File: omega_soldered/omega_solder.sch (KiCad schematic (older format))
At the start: 63 parts, among them SW1 SW_Push, U1 ProMicro

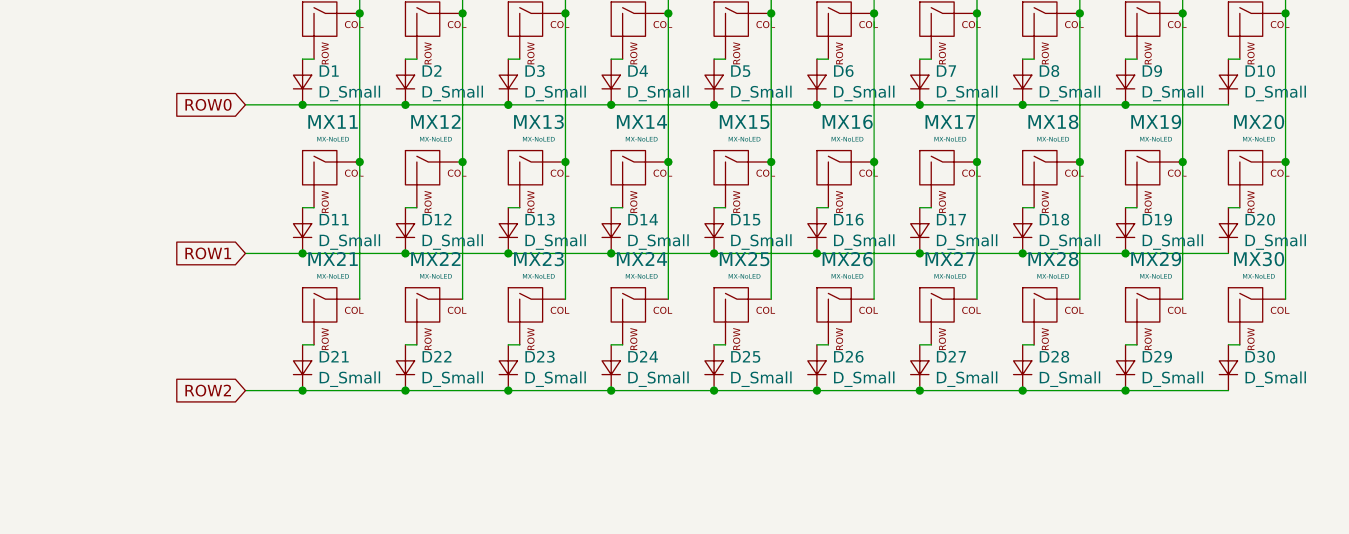
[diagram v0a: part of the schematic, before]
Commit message: add solder version
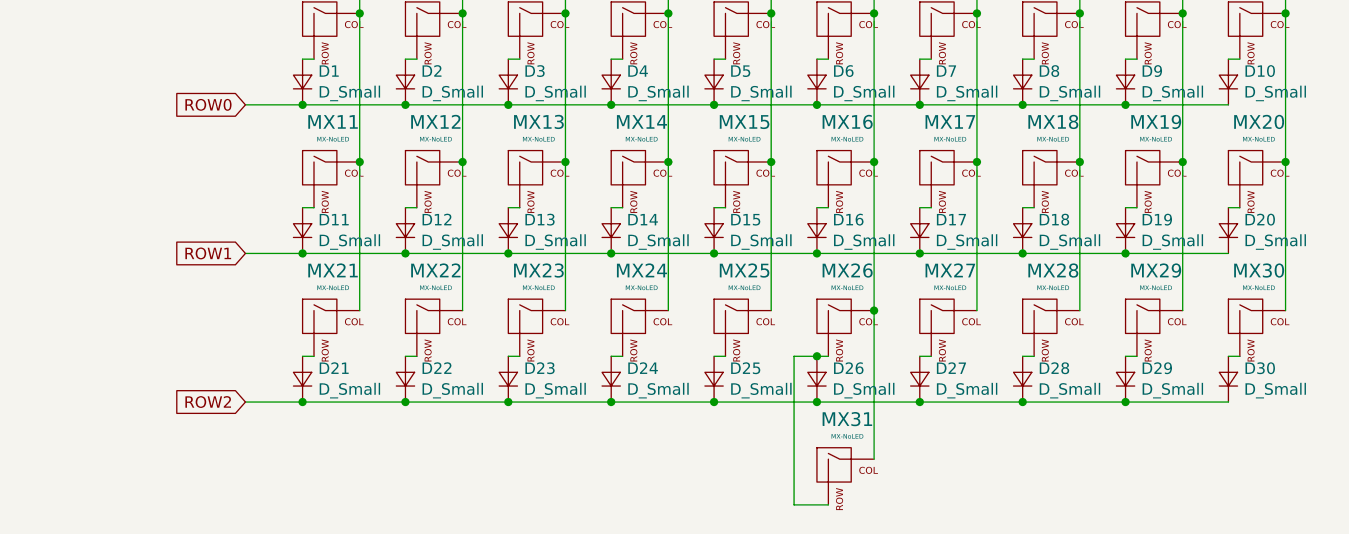
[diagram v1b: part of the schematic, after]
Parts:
- added MX31: MX-NoLED, MX_Only:MXOnly-2U-ReversedStabilizers-NoLED, symbol MX_Alps_Hybrid:MX-NoLED
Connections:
- net COL5: now also MX31.1 (COL)
- net at D26.2 (A), MX26.2 (ROW): now also MX31.2 (ROW)
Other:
- moved on the sheet: D21, D22, D23, D24, D25, D26, D27, D28, D29, D30, MX21, MX22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

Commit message: work
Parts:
- added H1, H2, H3, H4: Hole, MountingHole:MountingHole_2.2mm_M2, symbol keebio:Hole
- D1, D10, D11, D12, D13, D14, D15, D16, D17, D18, D19, D2, D20, D21, D22, D23, D24, D25, D26, D27, D28, D29, D3, D30, D4, D5, D6, D7, D8, D9: footprint Diode_THT:D_DO-35_SOD27_P3.81mm_Vertical_AnodeUp -> Keebio-Parts:Diode-Hybrid-Back
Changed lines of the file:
@@
 F 0 "D1" V 6146 1582 50  0000 R CNN
 F 1 "D_Small" V 6055 1582 50  0000 R CNN
-F 2 "Diode_THT:D_DO-35_SOD27_P3.81mm_Vertical_AnodeUp" V 6100 1650 50  0001 C CNN
+F 2 "Keebio-Parts:Diode-Hybrid-Back" V 6100 1650 50  0001 C CNN
 F 3 "~" V 6100 1650 50  0001 C CNN
 	1    6100 1650
@@
 F 0 "D11" V 6146 2232 50  0000 R CNN
 F 1 "D_Small" V 6055 2232 50  0000 R CNN
-F 2 "Diode_THT:D_DO-35_SOD27_P3.81mm_Vertical_AnodeUp" V 6100 2300 50  0001 C CNN
+F 2 "Keebio-Parts:Diode-Hybrid-Back" V 6100 2300 50  0001 C CNN
 F 3 "~" V 6100 2300 50  0001 C CNN
 	1    6100 2300
@@
 F 0 "D21" V 6146 2882 50  0000 R CNN
 F 1 "D_Small" V 6055 2882 50  0000 R CNN
-F 2 "Diode_THT:D_DO-35_SOD27_P3.81mm_Vertical_AnodeUp" V 6100 2950 50  0001 C CNN
+F 2 "Keebio-Parts:Diode-Hybrid-Back" V 6100 2950 50  0001 C CNN
 F 3 "~" V 6100 2950 50  0001 C CNN
 	1    6100 2950
@@
 F 0 "D2" V 6596 1582 50  0000 R CNN
 F 1 "D_Small" V 6505 1582 50  0000 R CNN
-F 2 "Diode_THT:D_DO-35_SOD27_P3.81mm_Vertical_AnodeUp" V 6550 1650 50  0001 C CNN
+F 2 "Keebio-Parts:Diode-Hybrid-Back" V 6550 1650 50  0001 C CNN
 F 3 "~" V 6550 1650 50  0001 C CNN
 	1    6550 1650
@@
 F 0 "D12" V 6596 2232 50  0000 R CNN
 F 1 "D_Small" V 6505 2232 50  0000 R CNN
-F 2 "Diode_THT:D_DO-35_SOD27_P3.81mm_Vertical_AnodeUp" V 6550 2300 50  0001 C CNN
+F 2 "Keebio-Parts:Diode-Hybrid-Back" V 6550 2300 50  0001 C CNN
 F 3 "~" V 6550 2300 50  0001 C CNN
 	1    6550 2300
@@
 F 0 "D22" V 6596 2882 50  0000 R CNN
 F 1 "D_Small" V 6505 2882 50  0000 R CNN
-F 2 "Diode_THT:D_DO-35_SOD27_P3.81mm_Vertical_AnodeUp" V 6550 2950 50  0001 C CNN
+F 2 "Keebio-Parts:Diode-Hybrid-Back" V 6550 2950 50  0001 C CNN
 F 3 "~" V 6550 2950 50  0001 C CNN
 	1    6550 2950
@@
 F 0 "D3" V 7046 1582 50  0000 R CNN
 F 1 "D_Small" V 6955 1582 50  0000 R CNN
-F 2 "Diode_THT:D_DO-35_SOD27_P3.81mm_Vertical_AnodeUp" V 7000 1650 50  0001 C CNN
+F 2 "Keebio-Parts:Diode-Hybrid-Back" V 7000 1650 50  0001 C CNN
 F 3 "~" V 7000 1650 50  0001 C CNN
 	1    7000 1650
@@
 F 0 "D13" V 7046 2232 50  0000 R CNN
 F 1 "D_Small" V 6955 2232 50  0000 R CNN
-F 2 "Diode_THT:D_DO-35_SOD27_P3.81mm_Vertical_AnodeUp" V 7000 2300 50  0001 C CNN
+F 2 "Keebio-Parts:Diode-Hybrid-Back" V 7000 2300 50  0001 C CNN
 F 3 "~" V 7000 2300 50  0001 C CNN
 	1    7000 2300
@@
 F 0 "D23" V 7046 2882 50  0000 R CNN
 F 1 "D_Small" V 6955 2882 50  0000 R CNN
-F 2 "Diode_THT:D_DO-35_SOD27_P3.81mm_Vertical_AnodeUp" V 7000 2950 50  0001 C CNN
+F 2 "Keebio-Parts:Diode-Hybrid-Back" V 7000 2950 50  0001 C CNN
 F 3 "~" V 7000 2950 50  0001 C CNN
 	1    7000 2950
@@
 F 0 "D4" V 7496 1582 50  0000 R CNN
 F 1 "D_Small" V 7405 1582 50  0000 R CNN
-F 2 "Diode_THT:D_DO-35_SOD27_P3.81mm_Vertical_AnodeUp" V 7450 1650 50  0001 C CNN
+F 2 "Keebio-Parts:Diode-Hybrid-Back" V 7450 1650 50  0001 C CNN
 F 3 "~" V 7450 1650 50  0001 C CNN
 	1    7450 1650
@@
 F 0 "D14" V 7496 2232 50  0000 R CNN
 F 1 "D_Small" V 7405 2232 50  0000 R CNN
-F 2 "Diode_THT:D_DO-35_SOD27_P3.81mm_Vertical_AnodeUp" V 7450 2300 50  0001 C CNN
+F 2 "Keebio-Parts:Diode-Hybrid-Back" V 7450 2300 50  0001 C CNN
 F 3 "~" V 7450 2300 50  0001 C CNN
 	1    7450 2300
@@
 F 0 "D24" V 7496 2882 50  0000 R CNN
 F 1 "D_Small" V 7405 2882 50  0000 R CNN
-F 2 "Diode_THT:D_DO-35_SOD27_P3.81mm_Vertical_AnodeUp" V 7450 2950 50  0001 C CNN
+F 2 "Keebio-Parts:Diode-Hybrid-Back" V 7450 2950 50  0001 C CNN
 F 3 "~" V 7450 2950 50  0001 C CNN
 	1    7450 2950
@@
 F 0 "D5" V 7946 1582 50  0000 R CNN
 F 1 "D_Small" V 7855 1582 50  0000 R CNN
-F 2 "Diode_THT:D_DO-35_SOD27_P3.81mm_Vertical_AnodeUp" V 7900 1650 50  0001 C CNN
+F 2 "Keebio-Parts:Diode-Hybrid-Back" V 7900 1650 50  0001 C CNN
 F 3 "~" V 7900 1650 50  0001 C CNN
 	1    7900 1650
@@
 F 0 "D15" V 7946 2232 50  0000 R CNN
 F 1 "D_Small" V 7855 2232 50  0000 R CNN
-F 2 "Diode_THT:D_DO-35_SOD27_P3.81mm_Vertical_AnodeUp" V 7900 2300 50  0001 C CNN
+F 2 "Keebio-Parts:Diode-Hybrid-Back" V 7900 2300 50  0001 C CNN
 F 3 "~" V 7900 2300 50  0001 C CNN
 	1    7900 2300
@@
 F 0 "D25" V 7946 2882 50  0000 R CNN
 F 1 "D_Small" V 7855 2882 50  0000 R CNN
-F 2 "Diode_THT:D_DO-35_SOD27_P3.81mm_Vertical_AnodeUp" V 7900 2950 50  0001 C CNN
+F 2 "Keebio-Parts:Diode-Hybrid-Back" V 7900 2950 50  0001 C CNN
 F 3 "~" V 7900 2950 50  0001 C CNN
 	1    7900 2950
@@
 F 0 "D6" V 8396 1582 50  0000 R CNN
 F 1 "D_Small" V 8305 1582 50  0000 R CNN
-F 2 "Diode_THT:D_DO-35_SOD27_P3.81mm_Vertical_AnodeUp" V 8350 1650 50  0001 C CNN
+F 2 "Keebio-Parts:Diode-Hybrid-Back" V 8350 1650 50  0001 C CNN
 F 3 "~" V 8350 1650 50  0001 C CNN
 	1    8350 1650
@@
 F 0 "D16" V 8396 2232 50  0000 R CNN
 F 1 "D_Small" V 8305 2232 50  0000 R CNN
-F 2 "Diode_THT:D_DO-35_SOD27_P3.81mm_Vertical_AnodeUp" V 8350 2300 50  0001 C CNN
+F 2 "Keebio-Parts:Diode-Hybrid-Back" V 8350 2300 50  0001 C CNN
 F 3 "~" V 8350 2300 50  0001 C CNN
 	1    8350 2300
@@
 F 0 "D7" V 8846 1582 50  0000 R CNN
 F 1 "D_Small" V 8755 1582 50  0000 R CNN
-F 2 "Diode_THT:D_DO-35_SOD27_P3.81mm_Vertical_AnodeUp" V 8800 1650 50  0001 C CNN
+F 2 "Keebio-Parts:Diode-Hybrid-Back" V 8800 1650 50  0001 C CNN
 F 3 "~" V 8800 1650 50  0001 C CNN
 	1    8800 1650
@@
 F 0 "D17" V 8846 2232 50  0000 R CNN
 F 1 "D_Small" V 8755 2232 50  0000 R CNN
-F 2 "Diode_THT:D_DO-35_SOD27_P3.81mm_Vertical_AnodeUp" V 8800 2300 50  0001 C CNN
+F 2 "Keebio-Parts:Diode-Hybrid-Back" V 8800 2300 50  0001 C CNN
 F 3 "~" V 8800 2300 50  0001 C CNN
 	1    8800 2300
@@
 F 0 "D27" V 8846 2882 50  0000 R CNN
 F 1 "D_Small" V 8755 2882 50  0000 R CNN
-F 2 "Diode_THT:D_DO-35_SOD27_P3.81mm_Vertical_AnodeUp" V 8800 2950 50  0001 C CNN
+F 2 "Keebio-Parts:Diode-Hybrid-Back" V 8800 2950 50  0001 C CNN
 F 3 "~" V 8800 2950 50  0001 C CNN
 	1    8800 2950
@@
 F 0 "D8" V 9296 1582 50  0000 R CNN
 F 1 "D_Small" V 9205 1582 50  0000 R CNN
-F 2 "Diode_THT:D_DO-35_SOD27_P3.81mm_Vertical_AnodeUp" V 9250 1650 50  0001 C CNN
+F 2 "Keebio-Parts:Diode-Hybrid-Back" V 9250 1650 50  0001 C CNN
 F 3 "~" V 9250 1650 50  0001 C CNN
 	1    9250 1650
@@
 F 0 "D18" V 9296 2232 50  0000 R CNN
 F 1 "D_Small" V 9205 2232 50  0000 R CNN
-F 2 "Diode_THT:D_DO-35_SOD27_P3.81mm_Vertical_AnodeUp" V 9250 2300 50  0001 C CNN
+F 2 "Keebio-Parts:Diode-Hybrid-Back" V 9250 2300 50  0001 C CNN
 F 3 "~" V 9250 2300 50  0001 C CNN
 	1    9250 2300
@@
 F 0 "D28" V 9296 2882 50  0000 R CNN
 F 1 "D_Small" V 9205 2882 50  0000 R CNN
-F 2 "Diode_THT:D_DO-35_SOD27_P3.81mm_Vertical_AnodeUp" V 9250 2950 50  0001 C CNN
+F 2 "Keebio-Parts:Diode-Hybrid-Back" V 9250 2950 50  0001 C CNN
 F 3 "~" V 9250 2950 50  0001 C CNN
 	1    9250 2950
@@
 F 0 "D9" V 9746 1582 50  0000 R CNN
 F 1 "D_Small" V 9655 1582 50  0000 R CNN
-F 2 "Diode_THT:D_DO-35_SOD27_P3.81mm_Vertical_AnodeUp" V 9700 1650 50  0001 C CNN
+F 2 "Keebio-Parts:Diode-Hybrid-Back" V 9700 1650 50  0001 C CNN
 F 3 "~" V 9700 1650 50  0001 C CNN
 	1    9700 1650
@@
 F 0 "D19" V 9746 2232 50  0000 R CNN
 F 1 "D_Small" V 9655 2232 50  0000 R CNN
-F 2 "Diode_THT:D_DO-35_SOD27_P3.81mm_Vertical_AnodeUp" V 9700 2300 50  0001 C CNN
+F 2 "Keebio-Parts:Diode-Hybrid-Back" V 9700 2300 50  0001 C CNN
 F 3 "~" V 9700 2300 50  0001 C CNN
 	1    9700 2300
@@
 F 0 "D29" V 9746 2882 50  0000 R CNN
 F 1 "D_Small" V 9655 2882 50  0000 R CNN
-F 2 "Diode_THT:D_DO-35_SOD27_P3.81mm_Vertical_AnodeUp" V 9700 2950 50  0001 C CNN
+F 2 "Keebio-Parts:Diode-Hybrid-Back" V 9700 2950 50  0001 C CNN
 F 3 "~" V 9700 2950 50  0001 C CNN
 	1    9700 2950
@@
 F 0 "D10" V 10196 1582 50  0000 R CNN
 F 1 "D_Small" V 10105 1582 50  0000 R CNN
-F 2 "Diode_THT:D_DO-35_SOD27_P3.81mm_Vertical_AnodeUp" V 10150 1650 50  0001 C CNN
+F 2 "Keebio-Parts:Diode-Hybrid-Back" V 10150 1650 50  0001 C CNN
 F 3 "~" V 10150 1650 50  0001 C CNN
 	1    10150 1650
@@
 F 0 "D20" V 10196 2232 50  0000 R CNN
 F 1 "D_Small" V 10105 2232 50  0000 R CNN
-F 2 "Diode_THT:D_DO-35_SOD27_P3.81mm_Vertical_AnodeUp" V 10150 2300 50  0001 C CNN
+F 2 "Keebio-Parts:Diode-Hybrid-Back" V 10150 2300 50  0001 C CNN
 F 3 "~" V 10150 2300 50  0001 C CNN
 	1    10150 2300
@@
 F 0 "D30" V 10196 2882 50  0000 R CNN
 F 1 "D_Small" V 10105 2882 50  0000 R CNN
-F 2 "Diode_THT:D_DO-35_SOD27_P3.81mm_Vertical_AnodeUp" V 10150 2950 50  0001 C CNN
+F 2 "Keebio-Parts:Diode-Hybrid-Back" V 10150 2950 50  0001 C CNN
 F 3 "~" V 10150 2950 50  0001 C CNN
 	1    10150 2950
@@
 F 0 "D26" V 8396 2882 50  0000 R CNN
 F 1 "D_Small" V 8305 2882 50  0000 R CNN
-F 2 "Diode_THT:D_DO-35_SOD27_P3.81mm_Vertical_AnodeUp" V 8350 2950 50  0001 C CNN
+F 2 "Keebio-Parts:Diode-Hybrid-Back" V 8350 2950 50  0001 C CNN
 F 3 "~" V 8350 2950 50  0001 C CNN
 	1    8350 2950
@@
 	9950 2000 9950 2650
 Connection ~ 9950 2000
+$Comp
+L keebio:Hole H1
+U 1 1 5F08444E
+P 4350 3500
+F 0 "H1" H 4536 3553 60  0000 L CNN
+F 1 "Hole" H 4536 3447 60  0000 L CNN
+F 2 "MountingHole:MountingHole_2.2mm_M2" H 4350 3500 60  0001 C CNN
+F 3 "" H 4350 3500 60  0001 C CNN
+	1    4350 3500
+	1    0    0    -1
+$EndComp
+$Comp
+L keebio:Hole H2
+U 1 1 5F084F55
+P 4950 3500
+F 0 "H2" H 5136 3553 60  0000 L CNN
+F 1 "Hole" H 5136 3447 60  0000 L CNN
+F 2 "MountingHole:MountingHole_2.2mm_M2" H 4950 3500 60  0001 C CNN
+F 3 "" H 4950 3500 60  0001 C CNN
+	1    4950 3500
+	1    0    0    -1
+$EndComp
+$Comp
+L keebio:Hole H4
+U 1 1 5F085599
+P 4950 3900
+F 0 "H4" H 5136 3953 60  0000 L CNN
+F 1 "Hole" H 5136 3847 60  0000 L CNN
+F 2 "MountingHole:MountingHole_2.2mm_M2" H 4950 3900 60  0001 C CNN
+F 3 "" H 4950 3900 60  0001 C CNN
+	1    4950 3900
+	1    0    0    -1
+$EndComp
+$Comp
+L keebio:Hole H3
+U 1 1 5F085CDC
+P 4350 3900
+F 0 "H3" H 4536 3953 60  0000 L CNN
+F 1 "Hole" H 4536 3847 60  0000 L CNN
+F 2 "MountingHole:MountingHole_2.2mm_M2" H 4350 3900 60  0001 C CNN
+F 3 "" H 4350 3900 60  0001 C CNN
+	1    4350 3900
+	1    0    0    -1
+$EndComp
 $EndSCHEMATC

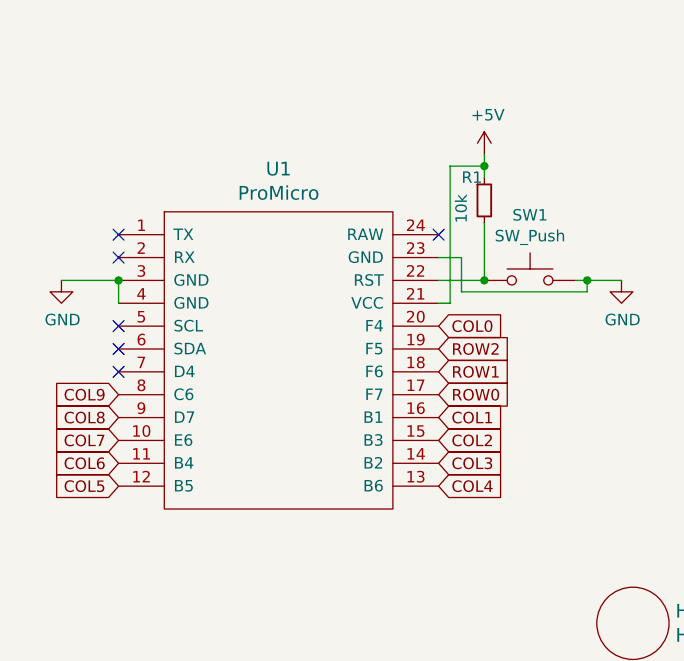
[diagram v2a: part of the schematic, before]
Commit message: update soldered omega
flip pro micro footprint
shuffle mounting holes
make stl files to 3D print for testing
regenerate gerbers
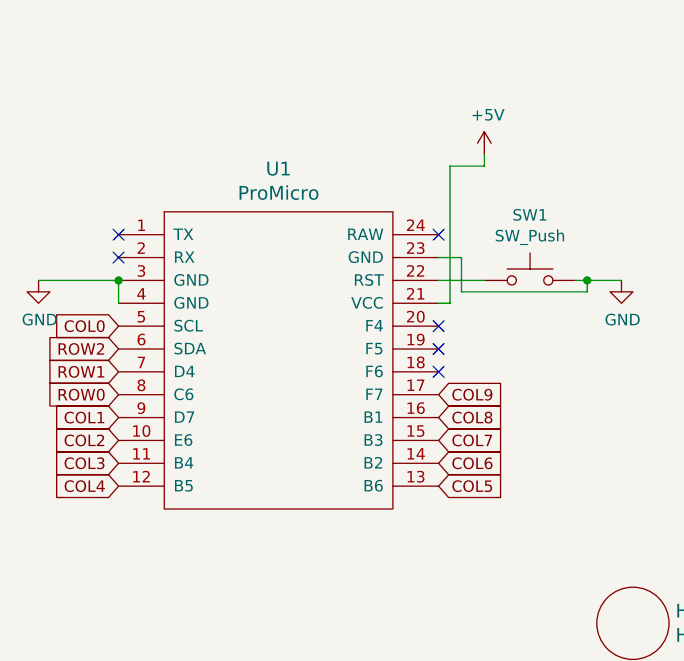
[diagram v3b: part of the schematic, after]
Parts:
- removed R1: 10k, Resistor_THT:R_Axial_DIN0204_L3.6mm_D1.6mm_P5.08mm_Horizontal, symbol Device:R_Small
- H1, H2, H3, H4: footprint MountingHole:MountingHole_2.2mm_M2 -> MountingHole:MountingHole_3.2mm_M3_ISO7380
- SW1: footprint random-keyboard-parts:SKQG-1155865 -> Button_Switch_SMD:SW_DIP_SPSTx01_Slide_Copal_CHS-01A_W5.08mm_P1.27mm_JPin
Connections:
- net COL0: now also U1.5 (SCL); no longer U1.20 (F4)
- net COL1: now also U1.9 (D7); no longer U1.16 (B1)
- net COL2: now also U1.10 (E6); no longer U1.15 (B3)
- net COL3: now also U1.11 (B4); no longer U1.14 (B2)
- net COL4: now also U1.12 (B5); no longer U1.13 (B6)
- net COL5: now also U1.13 (B6); no longer U1.12 (B5)
- net COL6: now also U1.14 (B2); no longer U1.11 (B4)
- net COL7: now also U1.15 (B3); no longer U1.10 (E6)
- net COL8: now also U1.16 (B1); no longer U1.9 (D7)
- net COL9: now also U1.17 (F7); no longer U1.8 (C6)
- net ROW0: now also U1.8 (C6); no longer U1.17 (F7)
- net ROW1: now also U1.7 (D4); no longer U1.18 (F6)
- net ROW2: now also U1.6 (SDA); no longer U1.19 (F5)
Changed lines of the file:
@@
 $EndComp
-Wire Wire Line
-	3700 1750 3700 2000
 Wire Wire Line
 	3700 1450 3700 1500
@@
 $EndComp
 $Comp
-L Device:R_Small R1
-U 1 1 5ED8D27E
-P 3700 1650
-F 0 "R1" H 3600 1750 50  0000 L CNN
-F 1 "10k" V 3600 1550 50  0000 L CNN
-F 2 "Resistor_THT:R_Axial_DIN0204_L3.6mm_D1.6mm_P5.08mm_Horizontal" H 3700 1650 50  0001 C CNN
-F 3 "~" H 3700 1650 50  0001 C CNN
-	1    3700 1650
-	1    0    0    -1
-$EndComp
-$Comp
 L Switch:SW_Push SW1
 U 1 1 5ED8D28E
@@
 F 0 "SW1" H 3900 2285 50  0000 C CNN
 F 1 "SW_Push" H 3900 2194 50  0000 C CNN
-F 2 "random-keyboard-parts:SKQG-1155865" H 3900 2200 50  0001 C CNN
+F 2 "Button_Switch_SMD:SW_DIP_SPSTx01_Slide_Copal_CHS-01A_W5.08mm_P1.27mm_JPin" H 3900 2200 50  0001 C CNN
 F 3 "~" H 3900 2200 50  0001 C CNN
 	1    3900 2000
@@
 Wire Wire Line
 	3700 2000 3500 2000
-Connection ~ 3700 2000
 Wire Wire Line
 	4300 2000 4150 2000
@@
 L power:GND #PWR02
 U 1 1 5EDC5385
-P 1850 2000
-F 0 "#PWR02" H 1850 1750 50  0001 C CNN
-F 1 "GND" H 1855 1827 50  0000 C CNN
-F 2 "" H 1850 2000 50  0001 C CNN
-F 3 "" H 1850 2000 50  0001 C CNN
-	1    1850 2000
-	1    0    0    -1
-$EndComp
-Wire Wire Line
-	1850 2000 2100 2000
+P 1750 2000
+F 0 "#PWR02" H 1750 1750 50  0001 C CNN
+F 1 "GND" H 1755 1827 50  0000 C CNN
+F 2 "" H 1750 2000 50  0001 C CNN
+F 3 "" H 1750 2000 50  0001 C CNN
+	1    1750 2000
+	1    0    0    -1
+$EndComp
 Wire Wire Line
 	2100 2000 2100 2100
-Connection ~ 2100 2000
 Wire Wire Line
 	3500 1900 3600 1900
@@
 Wire Wire Line
 	3550 1500 3700 1500
-Connection ~ 3700 1500
-Wire Wire Line
-	3700 1500 3700 1550
+Text GLabel 3500 2800 2    50   Input ~ 0
+COL6
+Text GLabel 2100 2600 0    50   Input ~ 0
+COL1
+Text GLabel 3500 2600 2    50   Input ~ 0
+COL8
+Text GLabel 3500 2500 2    50   Input ~ 0
+COL9
+Text GLabel 2100 2700 0    50   Input ~ 0
+COL2
+Text GLabel 2100 2500 0    50   Input ~ 0
+ROW0
+Text GLabel 2100 2200 0    50   Input ~ 0
+COL0
+Text GLabel 2100 2300 0    50   Input ~ 0
+ROW2
+Text GLabel 2100 2400 0    50   Input ~ 0
+ROW1
+Text GLabel 3500 2700 2    50   Input ~ 0
+COL7
+Text GLabel 3500 2900 2    50   Input ~ 0
+COL5
+Text GLabel 2100 2900 0    50   Input ~ 0
+COL4
 Text GLabel 2100 2800 0    50   Input ~ 0
-COL6
-Text GLabel 3500 2600 2    50   Input ~ 0
-COL1
-Text GLabel 2100 2600 0    50   Input ~ 0
-COL8
-Text GLabel 2100 2500 0    50   Input ~ 0
-COL9
-Text GLabel 3500 2700 2    50   Input ~ 0
-COL2
-Text GLabel 3500 2500 2    50   Input ~ 0
-ROW0
-Text GLabel 3500 2200 2    50   Input ~ 0
-COL0
-Text GLabel 3500 2300 2    50   Input ~ 0
-ROW2
-Text GLabel 3500 2400 2    50   Input ~ 0
-ROW1
-Text GLabel 2100 2700 0    50   Input ~ 0
-COL7
-Text GLabel 2100 2900 0    50   Input ~ 0
-COL5
-Text GLabel 3500 2900 2    50   Input ~ 0
-COL4
-Text GLabel 3500 2800 2    50   Input ~ 0
 COL3
-NoConn ~ 2100 2200
-NoConn ~ 2100 2300
-NoConn ~ 2100 2400
 NoConn ~ 2100 1900
 NoConn ~ 2100 1800
@@
 F 0 "H1" H 4536 3553 60  0000 L CNN
 F 1 "Hole" H 4536 3447 60  0000 L CNN
-F 2 "MountingHole:MountingHole_2.2mm_M2" H 4350 3500 60  0001 C CNN
+F 2 "MountingHole:MountingHole_3.2mm_M3_ISO7380" H 4350 3500 60  0001 C CNN
 F 3 "" H 4350 3500 60  0001 C CNN
 	1    4350 3500
@@
 F 0 "H2" H 5136 3553 60  0000 L CNN
 F 1 "Hole" H 5136 3447 60  0000 L CNN
-F 2 "MountingHole:MountingHole_2.2mm_M2" H 4950 3500 60  0001 C CNN
+F 2 "MountingHole:MountingHole_3.2mm_M3_ISO7380" H 4950 3500 60  0001 C CNN
 F 3 "" H 4950 3500 60  0001 C CNN
 	1    4950 3500
@@
 F 0 "H4" H 5136 3953 60  0000 L CNN
 F 1 "Hole" H 5136 3847 60  0000 L CNN
-F 2 "MountingHole:MountingHole_2.2mm_M2" H 4950 3900 60  0001 C CNN
+F 2 "MountingHole:MountingHole_3.2mm_M3_ISO7380" H 4950 3900 60  0001 C CNN
 F 3 "" H 4950 3900 60  0001 C CNN
 	1    4950 3900
@@
 F 0 "H3" H 4536 3953 60  0000 L CNN
 F 1 "Hole" H 4536 3847 60  0000 L CNN
-F 2 "MountingHole:MountingHole_2.2mm_M2" H 4350 3900 60  0001 C CNN
+F 2 "MountingHole:MountingHole_3.2mm_M3_ISO7380" H 4350 3900 60  0001 C CNN
 F 3 "" H 4350 3900 60  0001 C CNN
 	1    4350 3900
 	1    0    0    -1
 $EndComp
+Wire Wire Line
+	1750 2000 2100 2000
+Connection ~ 2100 2000
+NoConn ~ 3500 2200
+NoConn ~ 3500 2300
+NoConn ~ 3500 2400
 $EndSCHEMATC

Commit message: update soldered omega
increase stanoff hole size through the pcb
update stl files and step files
shuffle file locations
regenerate gerbers
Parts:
- H1, H2, H3, H4: footprint MountingHole:MountingHole_3.2mm_M3_ISO7380 -> MountingHole:MountingHole_3.5mm
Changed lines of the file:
@@
 F 0 "H1" H 4536 3553 60  0000 L CNN
 F 1 "Hole" H 4536 3447 60  0000 L CNN
-F 2 "MountingHole:MountingHole_3.2mm_M3_ISO7380" H 4350 3500 60  0001 C CNN
+F 2 "MountingHole:MountingHole_3.5mm" H 4350 3500 60  0001 C CNN
 F 3 "" H 4350 3500 60  0001 C CNN
 	1    4350 3500
@@
 F 0 "H2" H 5136 3553 60  0000 L CNN
 F 1 "Hole" H 5136 3447 60  0000 L CNN
-F 2 "MountingHole:MountingHole_3.2mm_M3_ISO7380" H 4950 3500 60  0001 C CNN
+F 2 "MountingHole:MountingHole_3.5mm" H 4950 3500 60  0001 C CNN
 F 3 "" H 4950 3500 60  0001 C CNN
 	1    4950 3500
@@
 F 0 "H4" H 5136 3953 60  0000 L CNN
 F 1 "Hole" H 5136 3847 60  0000 L CNN
-F 2 "MountingHole:MountingHole_3.2mm_M3_ISO7380" H 4950 3900 60  0001 C CNN
+F 2 "MountingHole:MountingHole_3.5mm" H 4950 3900 60  0001 C CNN
 F 3 "" H 4950 3900 60  0001 C CNN
 	1    4950 3900
@@
 F 0 "H3" H 4536 3953 60  0000 L CNN
 F 1 "Hole" H 4536 3847 60  0000 L CNN
-F 2 "MountingHole:MountingHole_3.2mm_M3_ISO7380" H 4350 3900 60  0001 C CNN
+F 2 "MountingHole:MountingHole_3.5mm" H 4350 3900 60  0001 C CNN
 F 3 "" H 4350 3900 60  0001 C CNN
 	1    4350 3900
